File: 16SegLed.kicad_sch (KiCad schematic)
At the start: 34 parts, among them J1 Conn_01x10, J2 Conn_01x10, J3 Conn_01x10, J4 Conn_01x06_Socket, J5 Conn_01x04_Pin, J6 Conn_01x04_Pin, SW1 SW_Push, SW2 SW_Push, U1 ESP32-S3-WROOM-1, U2 AMS1117-3.3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

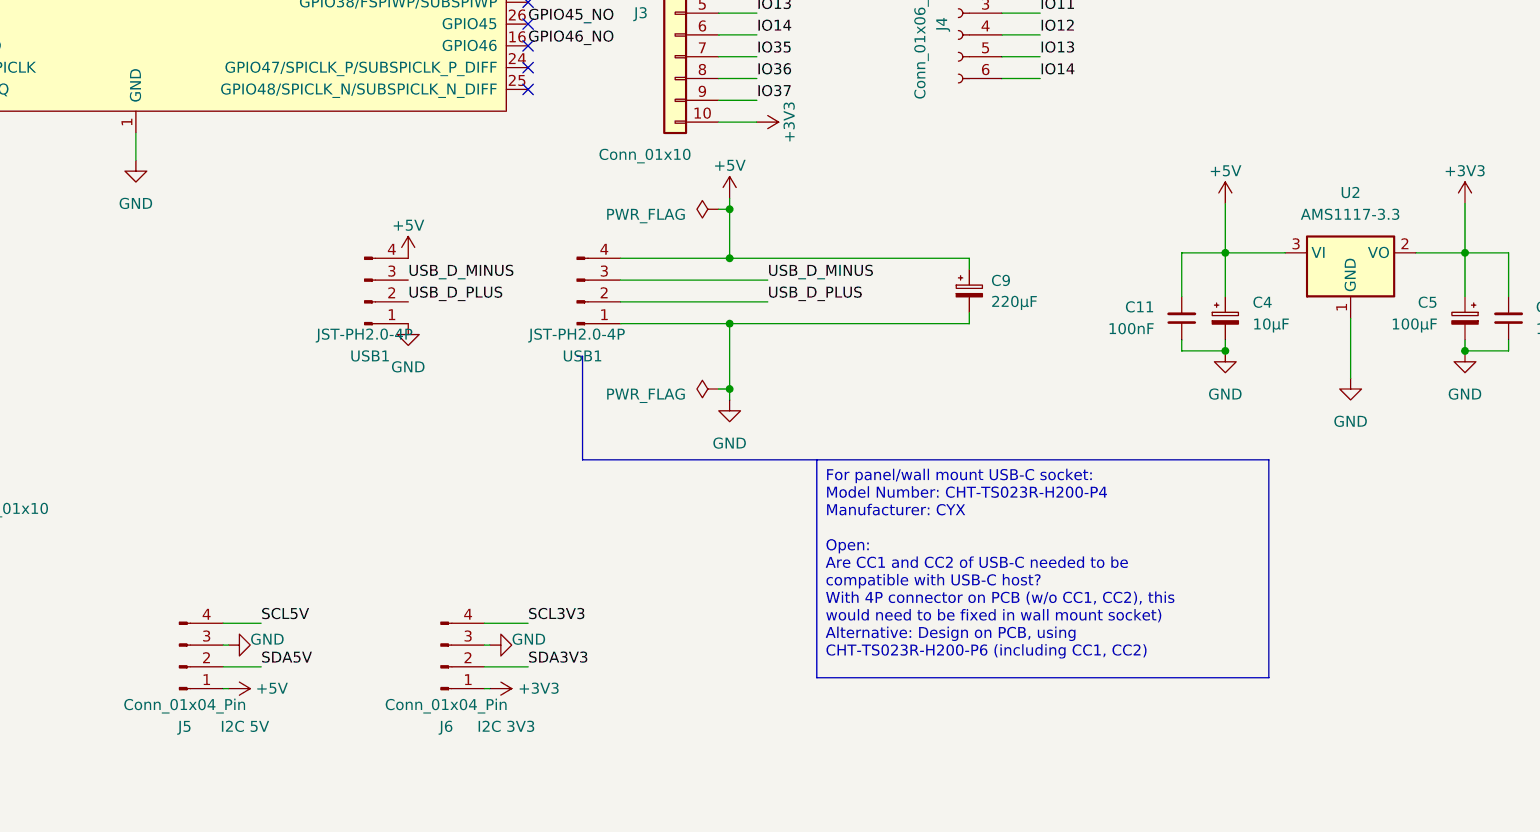
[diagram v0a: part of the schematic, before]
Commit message: Support native USB-C
- use 6P terminal for wall mount USB-C socket
- include 2x 5k1 resistors for CC1 and CC2
- larger footprints of connectors require partial re-layout
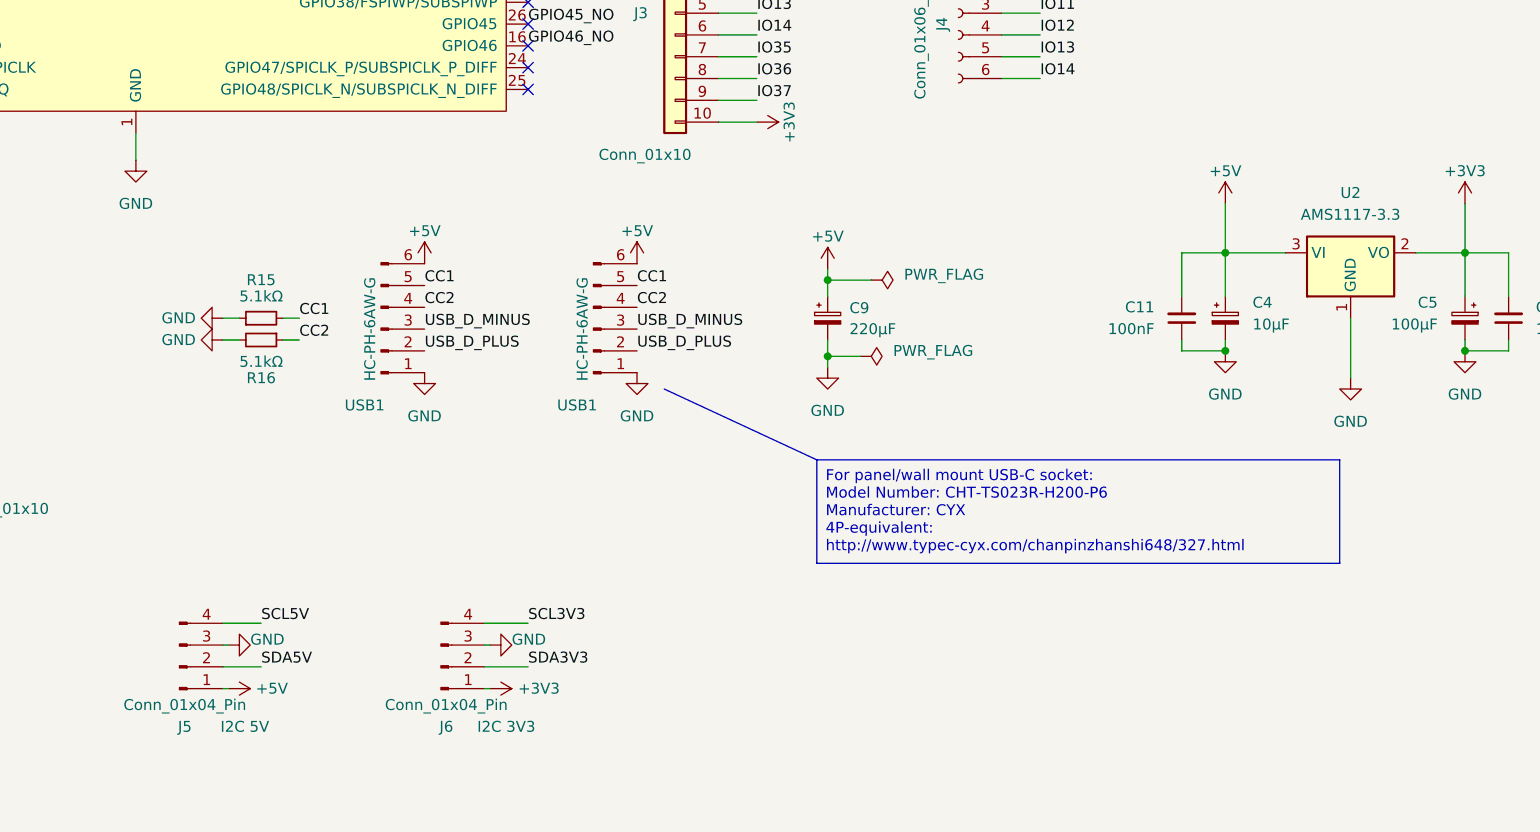
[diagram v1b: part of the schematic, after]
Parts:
- added R15, R16: 5.1kΩ, Resistor_SMD:R_0805_2012Metric, symbol Device:R_Small
- USB1: value JST-PH2.0-4P -> HC-PH-6AW-G; footprint ProjectLibrary:PH 1x04 P2.0 -> ProjectLibrary:PH 1x06 P2.0; symbol Connector:Conn_01x04_Pin -> Connector:Conn_01x06_Pin; LCSC C5342444 -> C5342446
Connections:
- net +5V: now also USB1.6 (Pin_6), USB1.6 (Pin_6); no longer USB1.4 (Pin_4), USB1.4 (Pin_4)
- net GND: now also R15.1, R16.2
- new net CC1: R15.2, USB1.5 (Pin_5), USB1.5 (Pin_5)
- new net CC2: R16.1, USB1.4 (Pin_4), USB1.4 (Pin_4)
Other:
- moved on the sheet: C9
